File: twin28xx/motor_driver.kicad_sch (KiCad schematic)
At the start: 21 parts, among them J9 Conn_01x03, U14 DRV8316CRRGFR

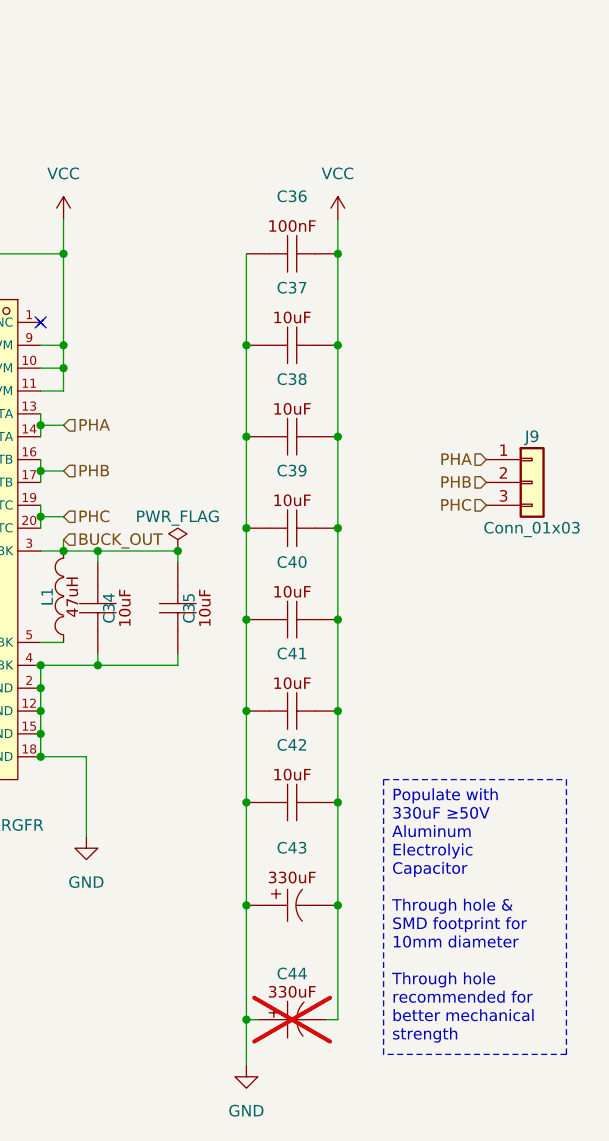
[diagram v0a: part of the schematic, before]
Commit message: swap bulk caps to VHXC hybrid, add second DRV8316 stage, relayout PCB
- motor_driver: replace 5x GRM21BR61H106KE43L bulk caps with 3x
  VHXC0581V101MVCG hybrid caps; add U14 (DRV8316CRRGFR), L1
  (PRS3015-470MT), R29, and associated decoupling (C38-44, C52, C61-66)
- PCB: relayout/reroute for the new parts
- refs: add Ymin VHXC and Chuanghui SV101M datasheets
- tools: add splitbank_sim.py power-delivery sim
- analysis: track manifest.json (outputs stay ignored)

Co-Authored-By: Claude Opus 5 (1M context) <noreply@anthropic.com>
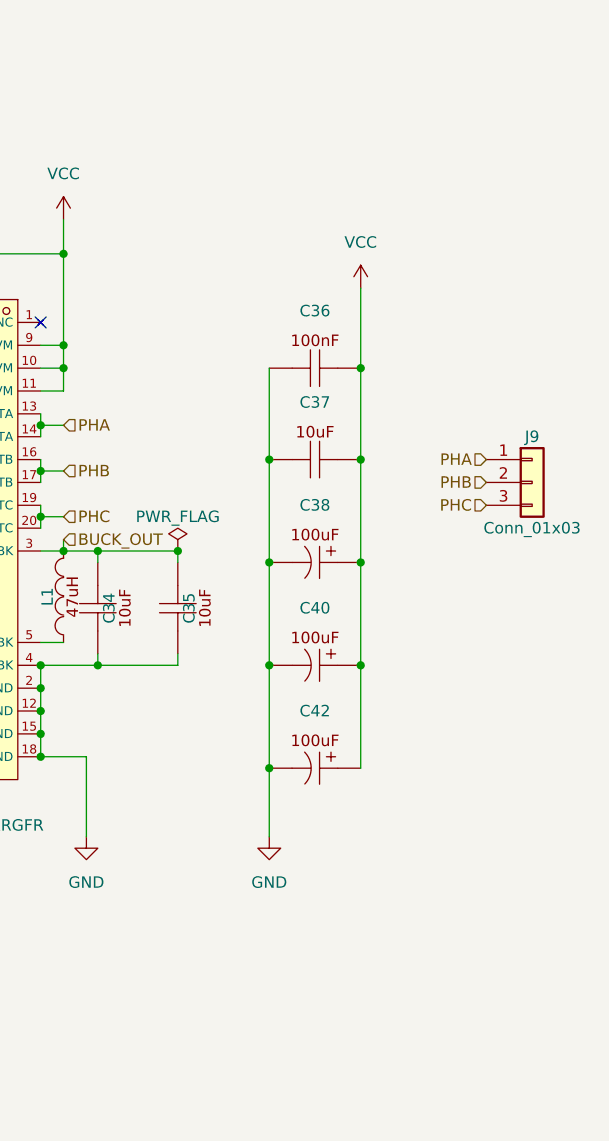
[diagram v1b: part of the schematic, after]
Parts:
- removed C38, C39, C40, C41, C42: GRM21BR61H106KE43L, Capacitor_SMD:C_0805_2012Metric, symbol Basic_Capacitors_Resistors:GRM21BR61H106KE43L
- removed C43: EEEFT1H331GP, Capacitor_SMD__C:CAP-SMD_BD10.0-L10.3-W10.3-LS11.0-R-RD, symbol Capacitor_SMD_UWRL:EEEFT1H331GP
- removed C44: 50PX330MEFC10X16, Capacitor_THT__C:CAP-TH_BD10.0-P5.00-D1.0-FD, symbol Capacitor_THT_UWRL:50PX330MEFC10X16
- added C38, C40, C42: VHXC0581V101MVCG, Capacitor_SMD:CP_Elec_6.3x5.8, symbol Capacitor_SMD__C:VHXC0581V101MVCG
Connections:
- net GND: now also C38.2, C40.2, C42.2
- net VCC: now also C38.1, C40.1, C42.1
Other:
- moved on the sheet: C36, C37
